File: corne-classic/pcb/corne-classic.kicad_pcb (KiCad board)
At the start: 2 copper layers, 133.8 x 92.2 mm, 91 parts, among them J1 MJ-4PP-9, J2 OLED, J3 LED, P1 i2c-pin, P2 i2c-pin, SW1 SW_PUSH, SW10 SW_PUSH, SW11 SW_PUSH, SW12 SW_PUSH, SW13 SW_PUSH, SW14 SW_PUSH, SW15 SW_PUSH, SW16 SW_PUSH, SW17 SW_PUSH, SW18 SW_PUSH, SW19 SW_PUSH, SW2 SW_PUSH, SW20 SW_PUSH, SW21 SW_PUSH, SW3 SW_PUSH, SW4 SW_PUSH, SW5 SW_PUSH, SW6 SW_PUSH, SW7 SW_PUSH, SW8 SW_PUSH, SW9 SW_PUSH, U1 ProMicro

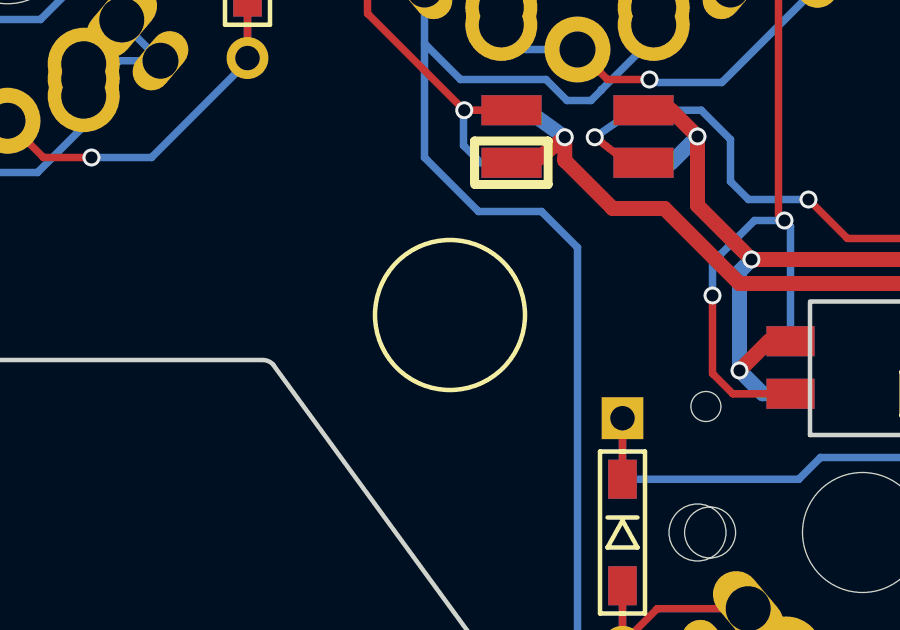
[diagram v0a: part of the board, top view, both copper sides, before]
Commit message: changed credits
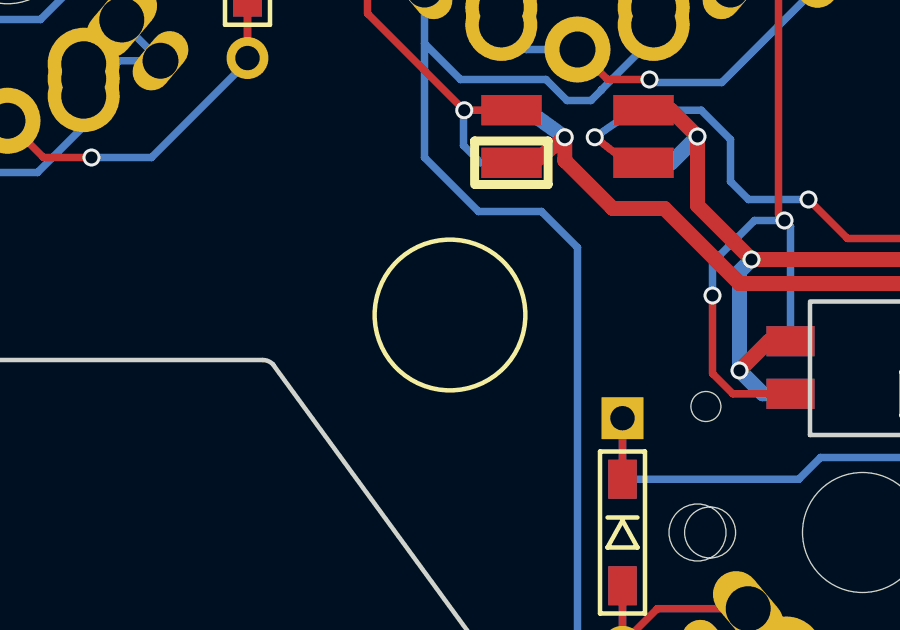
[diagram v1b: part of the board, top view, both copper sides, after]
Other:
- board text added: "Corne Classic 2.0 Caseless PCB by foostan ft. wy35"
- board text removed: "Corne Classic v2.0 PCB Designed by foostan"
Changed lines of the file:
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@@
     (35 F.Paste user hide)
     (36 B.SilkS user)
-    (37 F.SilkS user)
-    (38 B.Mask user hide)
-    (39 F.Mask user hide)
+    (37 F.SilkS user hide)
+    (38 B.Mask user)
+    (39 F.Mask user)
     (40 Dwgs.User user hide)
     (41 Cmts.User user hide)
     (42 Eco1.User user hide)
-    (43 Eco2.User user hide)
+    (43 Eco2.User user)
     (44 Edge.Cuts user)
     (45 Margin user hide)
@@
       (xy -5.296243 -4.794674)) (layer F.SilkS) (width 0.01))
   )
+  (gr_circle (center 122.75 122.75) (end 122.5 120.25) (layer F.SilkS) (width 0.15))
   (gr_circle (center 122.75 122.75) (end 122.5 120.25) (layer B.SilkS) (width 0.15))
   (gr_circle (center 169.25 130.500031) (end 169.262468 128.000031) (layer B.SilkS) (width 0.15))
-  (gr_circle (center 122.75 122.75) (end 122.75 120.25) (layer F.SilkS) (width 0.15))
   (gr_circle (center 79.5 86.762468) (end 79.25 84.262468) (layer F.SilkS) (width 0.15))
   (gr_circle (center 79.5 86.762468) (end 79.25 84.262468) (layer B.SilkS) (width 0.15))
@@
   )
   (target plus (at 194.8 63.4) (size 5) (width 0.15) (layer Edge.Cuts))
-  (gr_text "Corne Classic v2.0\nPCB Designed by foostan" (at 119.4 121.5) (layer B.Mask)
+  (gr_text "Corne Classic 2.0 Caseless\nPCB by foostan ft. wy35" (at 119.4 121.5) (layer B.Mask)
     (effects (font (size 1 1) (thickness 0.125)) (justify left mirror))
   )
-  (gr_text "Corne Classic v2.0\nPCB Designed by foostan" (at 100.1 121.5) (layer F.Mask)
+  (gr_text "Corne Classic 2.0 Caseless\nPCB by foostan ft. wy35" (at 99.5 121.5) (layer F.Mask)
     (effects (font (size 1 1) (thickness 0.125)) (justify left))
   )

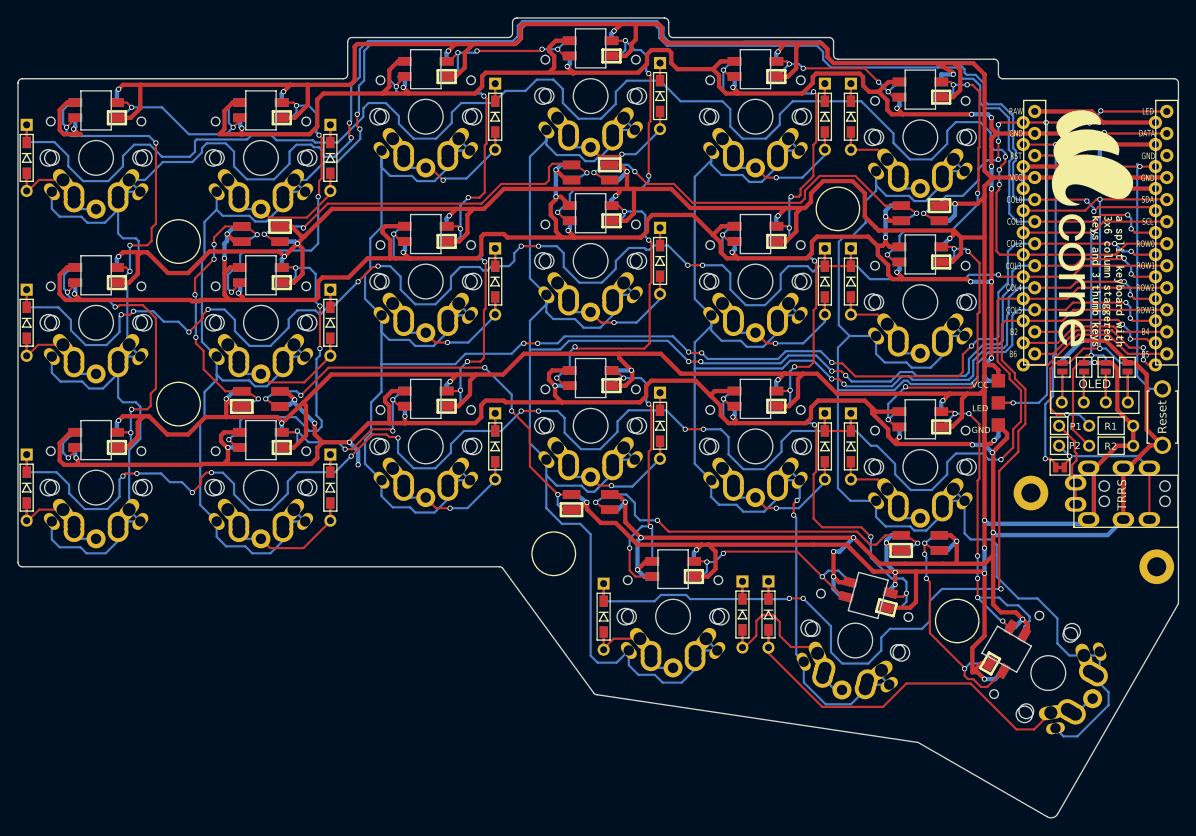
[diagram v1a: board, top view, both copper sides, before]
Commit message: added rubber feet areas
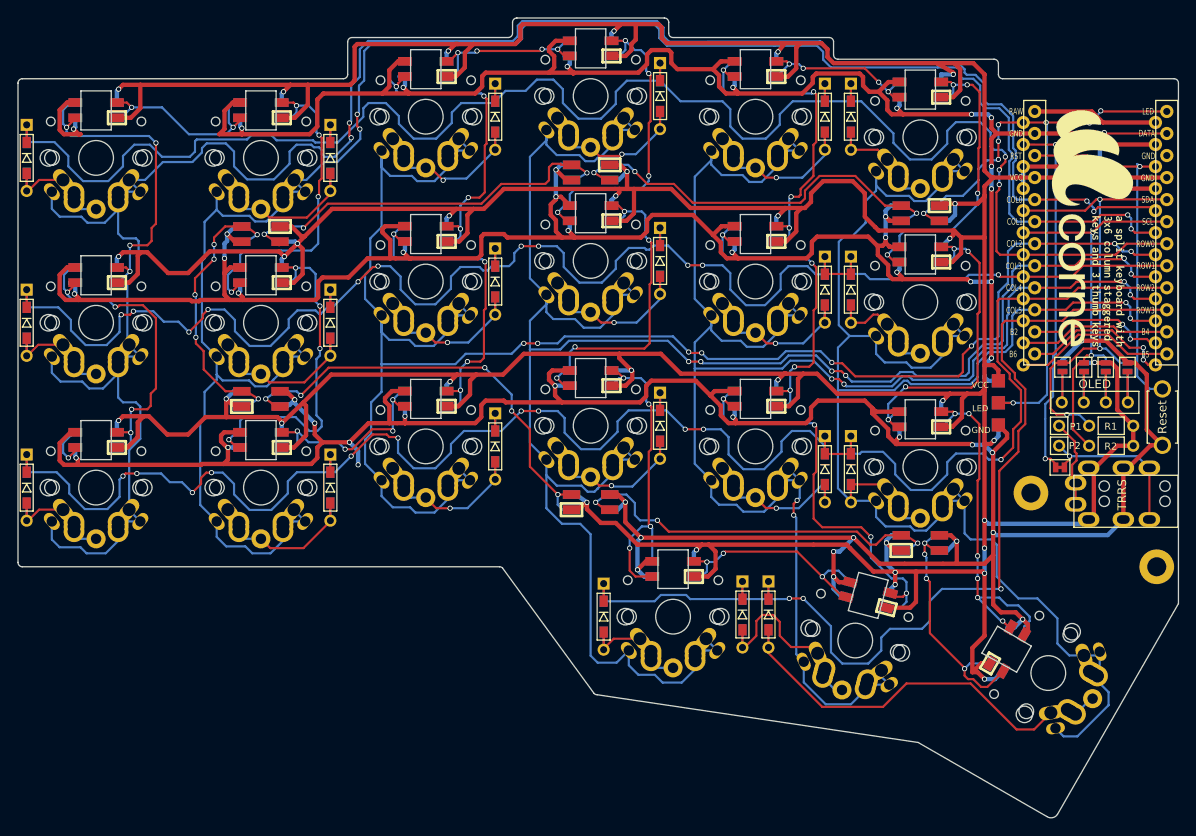
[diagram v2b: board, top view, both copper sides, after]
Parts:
- moved D17 2.62 mm to (154.0, 113.0)
- moved D18 2.62 mm to (157.0, 113.0)
- moved D11 0.94 mm to (154.0, 92.3)
- moved D12 0.94 mm to (157.0, 92.3)
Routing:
- net Net-(D18-Pad2): track 14.7 -> 13.1 mm
- net row2: track 215.8 -> 216.5 mm
- net Net-(D17-Pad2): track 20.4 -> 19.8 mm

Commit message: added ground plane
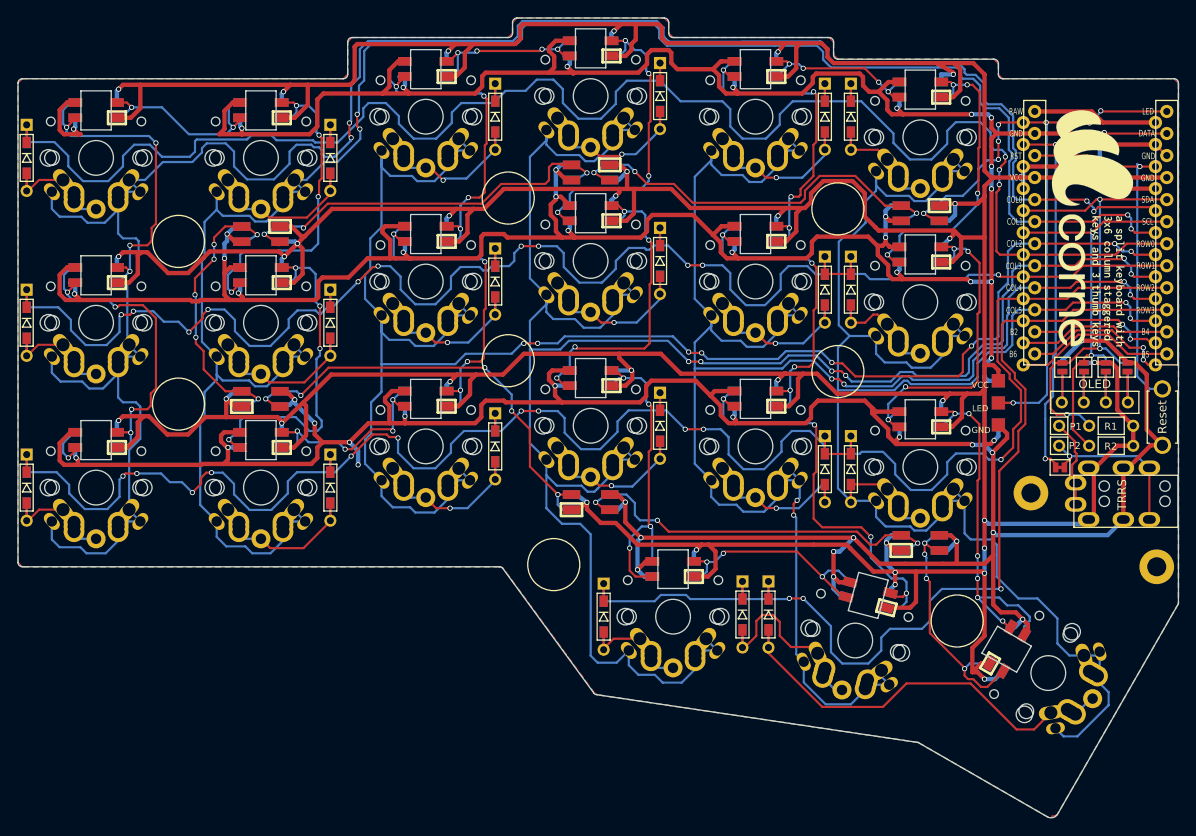
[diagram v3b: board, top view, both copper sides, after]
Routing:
- net GND: track 770.2 -> 772.0 mm
- added copper zone on B.Cu, net GND
- added copper zone on F.Cu, net GND
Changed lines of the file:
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@@
   (general
     (thickness 1.6)
-    (drawings 142)
-    (tracks 2914)
+    (drawings 150)
+    (tracks 2916)
     (zones 0)
     (modules 91)
@@
   )
   (layers
-    (0 F.Cu signal)
+    (0 F.Cu signal hide)
     (31 B.Cu signal)
     (32 B.Adhes user hide)
@@
     (35 F.Paste user hide)
     (36 B.SilkS user)
-    (37 F.SilkS user)
+    (37 F.SilkS user hide)
     (38 B.Mask user hide)
     (39 F.Mask user hide)
@@
       (drillshape 0)
       (scaleselection 1)
-      (outputdirectory "gerber/"))
+      (outputdirectory "../gerber/"))
   )
   (net 0 "")
@@
       (xy -5.296243 -4.794674)) (layer F.SilkS) (width 0.01))
   )
-  (gr_circle (center 117.5 81.75) (end 121.5 81.75) (layer B.SilkS) (width 0.15))
-  (gr_circle (center 117.5 100.5) (end 121.5 100.5) (layer B.SilkS) (width 0.15))
-  (gr_circle (center 155.5 101.75) (end 159.5 101.75) (layer B.SilkS) (width 0.15))
-  (gr_circle (center 155.5 83) (end 159.5 83) (layer B.SilkS) (width 0.15))
-  (gr_circle (center 79.5 86.75) (end 83.5 86.75) (layer B.SilkS) (width 0.15))
-  (gr_circle (center 79.5 105.5) (end 83.5 105.5) (layer B.SilkS) (width 0.15))
-  (gr_circle (center 169.25 130.5) (end 173.25 130.5) (layer B.SilkS) (width 0.15))
-  (gr_circle (center 122.75 124) (end 126.75 124) (layer B.SilkS) (width 0.15))
+  (gr_circle (center 169.25 130.5) (end 169.25 127.5) (layer F.SilkS) (width 0.15))
+  (gr_circle (center 155.5 101.75) (end 158.5 101.75) (layer F.SilkS) (width 0.15))
+  (gr_circle (center 155.5 83) (end 155.5 80) (layer F.SilkS) (width 0.15))
+  (gr_circle (center 117.5 81.75) (end 117.5 78.75) (layer F.SilkS) (width 0.15))
+  (gr_circle (center 122.75 124) (end 122.75 121) (layer F.SilkS) (width 0.15))
+  (gr_circle (center 117.5 100.5) (end 117.5 97.5) (layer F.SilkS) (width 0.15))
+  (gr_circle (center 79.5 105.5) (end 79.5 102.5) (layer F.SilkS) (width 0.15))
+  (gr_circle (center 79.5 86.75) (end 79.5 83.75) (layer F.SilkS) (width 0.15))
+  (gr_circle (center 117.5 81.75) (end 120.5 81.75) (layer B.SilkS) (width 0.15))
+  (gr_circle (center 117.5 100.5) (end 120.5 100.5) (layer B.SilkS) (width 0.15))
+  (gr_circle (center 155.5 101.75) (end 158.5 101.75) (layer B.SilkS) (width 0.15))
+  (gr_circle (center 155.5 83) (end 158.5 83) (layer B.SilkS) (width 0.15))
+  (gr_circle (center 79.5 86.75) (end 82.5 86.75) (layer B.SilkS) (width 0.15))
+  (gr_circle (center 79.5 105.5) (end 82.5 105.5) (layer B.SilkS) (width 0.15))
+  (gr_circle (center 169.25 130.5) (end 172.25 130.5) (layer B.SilkS) (width 0.15))
+  (gr_circle (center 122.75 124) (end 125.75 124) (layer B.SilkS) (width 0.15))
   (gr_text OLED (at 185.1 103.3) (layer B.SilkS)
     (effects (font (size 0.8128 0.8128) (thickness 0.15)) (justify mirror))
@@
   (segment (start 67.9 112.5) (end 82.1 112.5) (width 0.5) (layer F.Cu) (net 26))
   (segment (start 82.1 112.5) (end 82.2 112.4) (width 0.5) (layer F.Cu) (net 26))
+  (segment (start 193.37 76.852) (end 192.1 75.582) (width 0.25) (layer F.Cu) (net 26))
+  (segment (start 193.4064 76.852) (end 193.37 76.852) (width 0.25) (layer F.Cu) (net 26))
   (segment (start 161.1 121.5) (end 161.1 121.2) (width 0.5) (layer B.Cu) (net 27))
   (segment (start 161.675 120.625) (end 162.6 120.625) (width 0.5) (layer B.Cu) (net 27))
@@
   (segment (start 164.7 121.525) (end 163.325 120.625) (width 0.25) (layer F.Cu) (net 76))
   (via (at 164.7 121.525) (size 0.6) (drill 0.4) (layers F.Cu B.Cu) (net 76))
+  (zone (net 26) (net_name GND) (layer F.Cu) (hatch edge 0.508)
+    (connect_pads (clearance 0.508))
+    (min_thickness 0.254)
+    (fill yes (arc_segments 32) (thermal_gap 0.508) (thermal_bridge_width 0.508))
+    (polygon
+      (pts
+        (xy 136 61.5) (xy 136 62.75) (xy 136.5 63.25) (xy 154.5 63.25) (xy 155 63.75)
+        (xy 155 65.25) (xy 155.5 65.75) (xy 173.5 65.75) (xy 174 66.25) (xy 174 67.5)
+        (xy 174.5 68) (xy 194.25 68) (xy 194.75 68.5) (xy 194.75 128.5) (xy 180.75 152.875)
+        (xy 179.75 153.125) (xy 164.75 144.5) (xy 127.75 139) (xy 127.5 138.875) (xy 116.875 124.375)
+        (xy 116.5 124.25) (xy 61.5 124.25) (xy 61 123.75) (xy 61 68.5) (xy 61.5 68)
+        (xy 98.5 68) (xy 99 67.5) (xy 99 63.75) (xy 99.5 63.25) (xy 117.5 63.25)
+        (xy 118 62.75) (xy 118 61.5) (xy 118.5 61) (xy 135.5 61)
+      )
+    )
+  )
+  (zone (net 26) (net_name GND) (layer B.Cu) (hatch edge 0.508)
+    (connect_pads (clearance 0.508))
+    (min_thickness 0.254)
+    (fill yes (arc_segments 32) (thermal_gap 0.508) (thermal_bridge_width 0.508))
+    (polygon
+      (pts
+        (xy 136 61.5) (xy 136 62.75) (xy 136.5 63.25) (xy 154.5 63.25) (xy 155 63.75)
+        (xy 155 65.25) (xy 155.5 65.75) (xy 173.5 65.75) (xy 174 66.25) (xy 174 67.625)
+        (xy 174.5 68) (xy 194.25 68) (xy 194.75 68.5) (xy 194.75 128.5) (xy 180.75 152.875)
+        (xy 179.75 153.125) (xy 164.75 144.5) (xy 127.75 139) (xy 127.375 138.75) (xy 116.875 124.375)
+        (xy 116.5 124.25) (xy 61.5 124.25) (xy 61 123.75) (xy 61 68.5) (xy 61.5 68)
+        (xy 98.5 68) (xy 99 67.5) (xy 99 63.75) (xy 99.5 63.25) (xy 117.5 63.25)
+        (xy 118 62.75) (xy 118 61.5) (xy 118.5 61) (xy 135.5 61)
+      )
+    )
+  )
 )

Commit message: fix critical err: track goes thru resistor hole
and fixed tracks too close to board edge
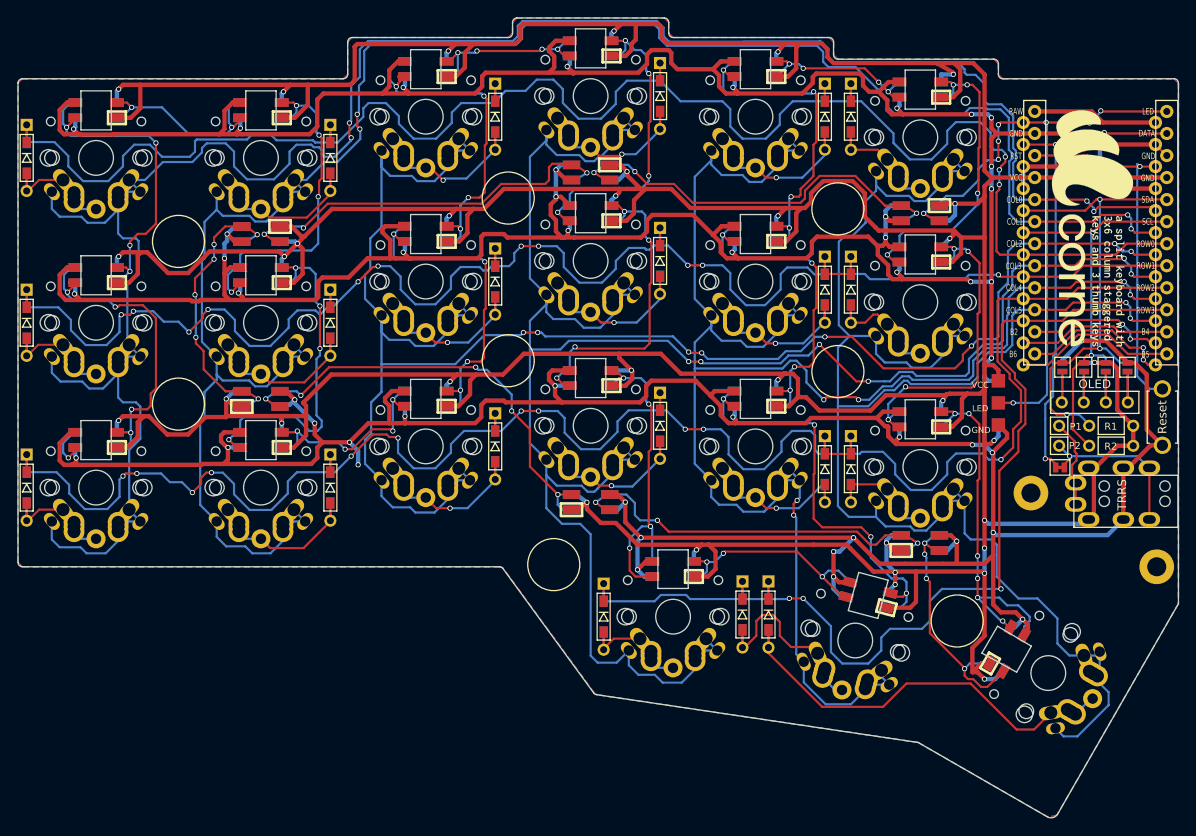
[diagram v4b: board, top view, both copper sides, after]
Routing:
- net GND: track 772.0 -> 785.0 mm
- net col5: track 187.0 -> 189.8 mm
- net col4: track 194.3 -> 196.6 mm
- net VCC: track 724.3 -> 726.0 mm
- net row2: track 216.5 -> 217.9 mm
- net col3: track 225.1 -> 226.1 mm
- net Net-(L1-Pad1): track 37.7 -> 37.1 mm
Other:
- outline, holes or cut-outs redrawn

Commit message: added extra foot silkscreen
and added my full name xd
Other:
- board text added: "Corne Classic 2.0 Caseless PCB by foostan ft. Will Ye"
- board text removed: "Corne Classic 2.0 Caseless PCB by foostan ft. wy35"
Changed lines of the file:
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@@
   (general
     (thickness 1.6)
-    (drawings 150)
+    (drawings 152)
     (tracks 2938)
     (zones 0)
@@
   )
   (layers
-    (0 F.Cu signal)
-    (31 B.Cu signal)
+    (0 F.Cu signal hide)
+    (31 B.Cu signal hide)
     (32 B.Adhes user hide)
     (33 F.Adhes user hide)
     (34 B.Paste user hide)
     (35 F.Paste user hide)
-    (36 B.SilkS user hide)
-    (37 F.SilkS user hide)
+    (36 B.SilkS user)
+    (37 F.SilkS user)
     (38 B.Mask user hide)
     (39 F.Mask user hide)
@@
       (xy -5.296243 -4.794674)) (layer F.SilkS) (width 0.01))
   )
+  (gr_circle (center 185 83) (end 188 83) (layer B.SilkS) (width 0.15))
+  (gr_circle (center 185 83) (end 188 83) (layer F.SilkS) (width 0.15))
   (gr_circle (center 169.25 130.5) (end 169.25 127.5) (layer F.SilkS) (width 0.15))
   (gr_circle (center 155.5 101.75) (end 158.5 101.75) (layer F.SilkS) (width 0.15))
@@
   )
   (target plus (at 194.8 63.4) (size 5) (width 0.15) (layer Edge.Cuts))
-  (gr_text "Corne Classic 2.0 Caseless\nPCB by foostan ft. wy35" (at 119.75 121.5) (layer B.Mask)
+  (gr_text "Corne Classic 2.0 Caseless\nPCB by foostan ft. Will Ye" (at 119.75 121.5) (layer B.Mask)
     (effects (font (size 1 1) (thickness 0.125)) (justify left mirror))
   )
-  (gr_text "Corne Classic 2.0 Caseless\nPCB by foostan ft. wy35" (at 99.5 121.5) (layer F.Mask)
+  (gr_text "Corne Classic 2.0 Caseless\nPCB by foostan ft. Will Ye" (at 99.5 121.5) (layer F.Mask)
     (effects (font (size 1 1) (thickness 0.125)) (justify left))
   )
